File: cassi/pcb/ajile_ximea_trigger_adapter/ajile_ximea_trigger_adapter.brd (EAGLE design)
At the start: 27.9 x 57.6 mm, 10 parts, among them K1 694108105102

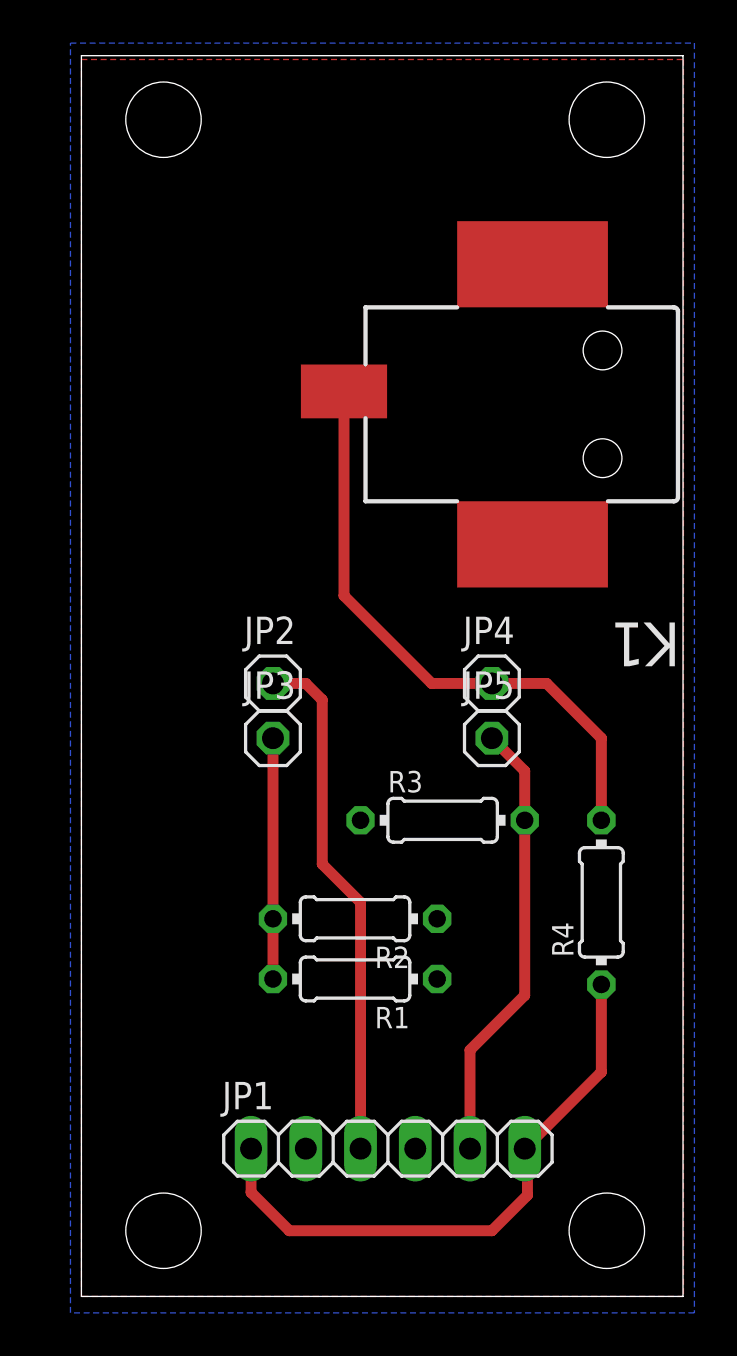
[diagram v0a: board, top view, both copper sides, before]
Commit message: put barrel jack on other side
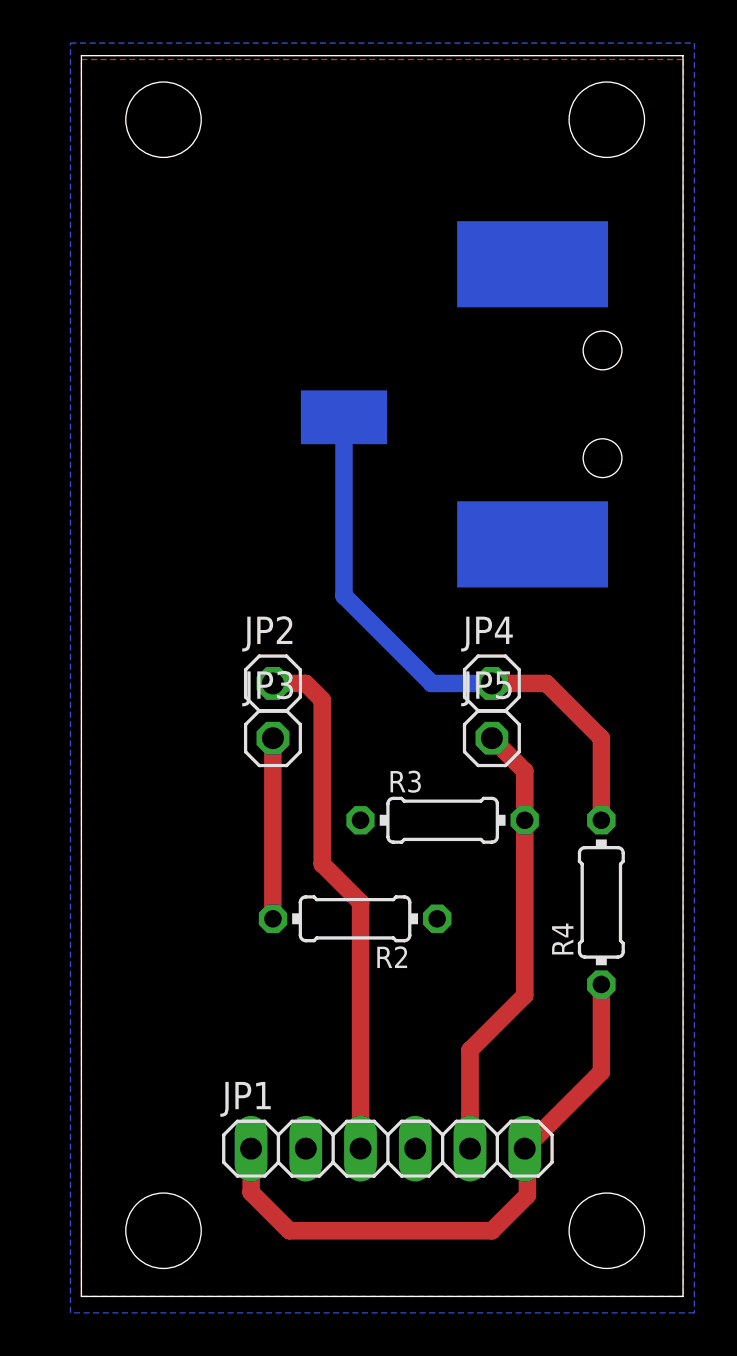
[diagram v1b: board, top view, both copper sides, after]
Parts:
- removed R1: 100, rcl:0204/7
- flipped K1 to the bottom, turned to 0 degrees
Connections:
- new net N$1: K1.2
- new net N$3: K1.3
- net GND: no longer K1.2, K1.3, R1.1
- net N$2: no longer R1.2
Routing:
- net N$2: track 11.2 -> 8.38 mm
- net 5V: track 28.0 -> 26.8 mm
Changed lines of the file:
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@@
 <elements>
 <element name="JP1" library="pinhead" library_urn="urn:adsk.eagle:library:325" package="1X06" package3d_urn="urn:adsk.eagle:package:22472/2" value="" x="14.224" y="6.858"/>
-<element name="K1" library="Wurth_Elektronik_Electromechanic_DC_Power_Jack_Connectors_rev15c" package="694108105102" value="694108105102" x="27.686" y="41.402" rot="R180"/>
+<element name="K1" library="Wurth_Elektronik_Electromechanic_DC_Power_Jack_Connectors_rev15c" package="694108105102" value="694108105102" x="27.686" y="41.402" rot="MR0"/>
 <element name="JP2" library="pinhead" library_urn="urn:adsk.eagle:library:325" package="1X01" package3d_urn="urn:adsk.eagle:package:22485/2" value="" x="8.89" y="28.448"/>
 <element name="JP3" library="pinhead" library_urn="urn:adsk.eagle:library:325" package="1X01" package3d_urn="urn:adsk.eagle:package:22485/2" value="" x="8.89" y="25.908"/>
 <element name="JP4" library="pinhead" library_urn="urn:adsk.eagle:library:325" package="1X01" package3d_urn="urn:adsk.eagle:package:22485/2" value="" x="19.05" y="28.448"/>
 <element name="JP5" library="pinhead" library_urn="urn:adsk.eagle:library:325" package="1X01" package3d_urn="urn:adsk.eagle:package:22485/2" value="" x="19.05" y="25.908"/>
-<element name="R1" library="rcl" library_urn="urn:adsk.eagle:library:334" package="0204/7" package3d_urn="urn:adsk.eagle:package:23498/1" value="100" x="12.7" y="14.732" rot="R180">
-<attribute name="SPICEPREFIX" value="R" x="12.7" y="14.732" size="1.778" layer="27" rot="R180" display="off"/>
-</element>
 <element name="R2" library="rcl" library_urn="urn:adsk.eagle:library:334" package="0204/7" package3d_urn="urn:adsk.eagle:package:23498/1" value="100" x="12.7" y="17.526" rot="R180">
 <attribute name="SPICEPREFIX" value="R" x="12.7" y="17.526" size="1.778" layer="27" rot="R180" display="off"/>
@@
 <contactref element="JP5" pad="1"/>
 <contactref element="R3" pad="2"/>
-<wire x1="20.574" y1="22.098" x2="20.574" y2="24.384" width="0.508" layer="1"/>
-<wire x1="20.574" y1="24.384" x2="19.05" y2="25.908" width="0.508" layer="1"/>
-<wire x1="20.574" y1="22.098" x2="20.574" y2="13.97" width="0.508" layer="1"/>
-<wire x1="20.574" y1="13.97" x2="18.034" y2="11.43" width="0.508" layer="1"/>
-<wire x1="18.034" y1="11.43" x2="18.034" y2="6.858" width="0.508" layer="1"/>
+<wire x1="20.574" y1="22.098" x2="20.574" y2="24.384" width="0.8128" layer="1"/>
+<wire x1="20.574" y1="24.384" x2="19.05" y2="25.908" width="0.8128" layer="1"/>
+<wire x1="20.574" y1="22.098" x2="20.574" y2="13.97" width="0.8128" layer="1"/>
+<wire x1="20.574" y1="13.97" x2="18.034" y2="11.43" width="0.8128" layer="1"/>
+<wire x1="18.034" y1="11.43" x2="18.034" y2="6.858" width="0.8128" layer="1"/>
 </signal>
 <signal name="AJILE_OUT">
 <contactref element="JP1" pad="3"/>
 <contactref element="JP2" pad="1"/>
-<wire x1="8.89" y1="28.448" x2="10.414" y2="28.448" width="0.508" layer="1"/>
-<wire x1="10.414" y1="28.448" x2="11.176" y2="27.686" width="0.508" layer="1"/>
-<wire x1="11.176" y1="27.686" x2="11.176" y2="20.066" width="0.508" layer="1"/>
-<wire x1="11.176" y1="20.066" x2="12.954" y2="18.288" width="0.508" layer="1"/>
-<wire x1="12.954" y1="18.288" x2="12.954" y2="6.858" width="0.508" layer="1"/>
+<wire x1="8.89" y1="28.448" x2="10.414" y2="28.448" width="0.8128" layer="1"/>
+<wire x1="10.414" y1="28.448" x2="11.176" y2="27.686" width="0.8128" layer="1"/>
+<wire x1="11.176" y1="27.686" x2="11.176" y2="20.066" width="0.8128" layer="1"/>
+<wire x1="11.176" y1="20.066" x2="12.954" y2="18.288" width="0.8128" layer="1"/>
+<wire x1="12.954" y1="18.288" x2="12.954" y2="6.858" width="0.8128" layer="1"/>
 </signal>
 <signal name="AJILE_IN">
@@
 <contactref element="JP1" pad="6"/>
 <contactref element="R4" pad="1"/>
-<wire x1="24.13" y1="14.478" x2="24.13" y2="10.414" width="0.508" layer="1"/>
-<wire x1="24.13" y1="10.414" x2="20.701" y2="6.985" width="0.508" layer="1"/>
+<wire x1="24.13" y1="14.478" x2="24.13" y2="10.414" width="0.8128" layer="1"/>
+<wire x1="24.13" y1="10.414" x2="20.701" y2="6.985" width="0.8128" layer="1"/>
 <wire x1="20.701" y1="6.985" x2="20.574" y2="6.858" width="0.508" layer="1"/>
-<wire x1="7.874" y1="6.858" x2="7.874" y2="4.826" width="0.508" layer="1"/>
-<wire x1="7.874" y1="4.826" x2="9.652" y2="3.048" width="0.508" layer="1"/>
-<wire x1="9.652" y1="3.048" x2="19.05" y2="3.048" width="0.508" layer="1"/>
-<wire x1="20.701" y1="4.699" x2="20.701" y2="6.985" width="0.508" layer="1"/>
-<wire x1="19.05" y1="3.048" x2="20.701" y2="4.699" width="0.508" layer="1"/>
+<wire x1="7.874" y1="6.858" x2="7.874" y2="4.826" width="0.8128" layer="1"/>
+<wire x1="7.874" y1="4.826" x2="9.652" y2="3.048" width="0.8128" layer="1"/>
+<wire x1="9.652" y1="3.048" x2="19.05" y2="3.048" width="0.8128" layer="1"/>
+<wire x1="20.701" y1="4.699" x2="20.701" y2="6.985" width="0.8128" layer="1"/>
+<wire x1="19.05" y1="3.048" x2="20.701" y2="4.699" width="0.8128" layer="1"/>
 </signal>
 <signal name="GND">
-<contactref element="K1" pad="2"/>
-<contactref element="K1" pad="3"/>
 <contactref element="JP1" pad="4"/>
 <contactref element="JP1" pad="2"/>
-<contactref element="R1" pad="1"/>
 <contactref element="R2" pad="1"/>
 <contactref element="R3" pad="1"/>
@@
 <contactref element="JP4" pad="1"/>
 <contactref element="R4" pad="2"/>
-<wire x1="12.186" y1="42.002" x2="12.186" y2="32.518" width="0.508" layer="1"/>
-<wire x1="12.186" y1="32.518" x2="16.256" y2="28.448" width="0.508" layer="1"/>
-<wire x1="16.256" y1="28.448" x2="19.05" y2="28.448" width="0.508" layer="1"/>
-<wire x1="19.05" y1="28.448" x2="21.59" y2="28.448" width="0.508" layer="1"/>
-<wire x1="21.59" y1="28.448" x2="24.13" y2="25.908" width="0.508" layer="1"/>
-<wire x1="24.13" y1="25.908" x2="24.13" y2="22.098" width="0.508" layer="1"/>
+<wire x1="12.186" y1="40.802" x2="12.186" y2="32.518" width="0.8128" layer="16"/>
+<wire x1="19.05" y1="28.448" x2="21.59" y2="28.448" width="0.8128" layer="1"/>
+<wire x1="21.59" y1="28.448" x2="24.13" y2="25.908" width="0.8128" layer="1"/>
+<wire x1="24.13" y1="25.908" x2="24.13" y2="22.098" width="0.8128" layer="1"/>
+<wire x1="12.186" y1="32.518" x2="16.256" y2="28.448" width="0.8128" layer="16"/>
+<wire x1="16.256" y1="28.448" x2="19.05" y2="28.448" width="0.8128" layer="16"/>
 </signal>
 <signal name="N$2">
-<contactref element="R1" pad="2"/>
 <contactref element="R2" pad="2"/>
 <contactref element="JP3" pad="1"/>
-<wire x1="8.89" y1="25.908" x2="8.89" y2="17.526" width="0.508" layer="1"/>
-<wire x1="8.89" y1="17.526" x2="8.89" y2="14.732" width="0.508" layer="1"/>
+<wire x1="8.89" y1="25.908" x2="8.89" y2="17.526" width="0.8128" layer="1"/>
+</signal>
+<signal name="N$1">
+<contactref element="K1" pad="2"/>
+</signal>
+<signal name="N$3">
+<contactref element="K1" pad="3"/>
 </signal>
 </signals>

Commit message: finished new ajile adapter pcb and added libraries used
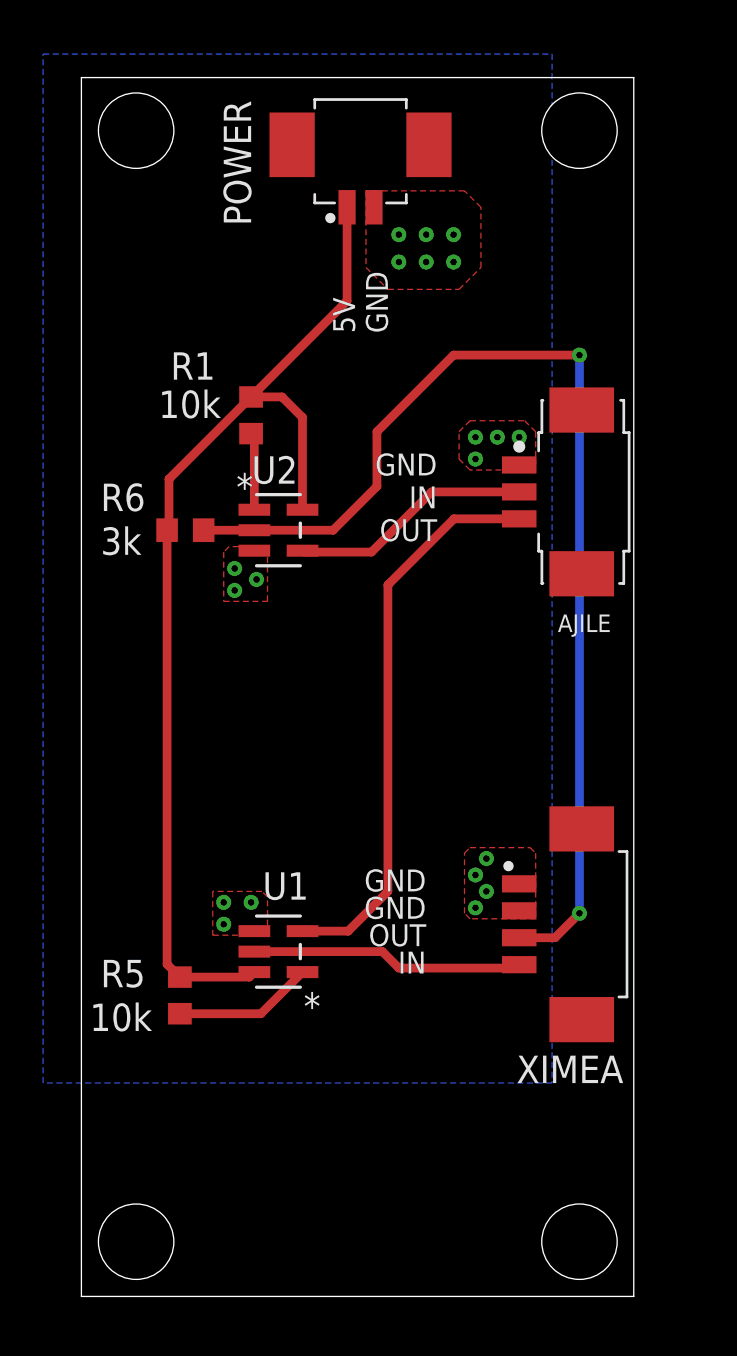
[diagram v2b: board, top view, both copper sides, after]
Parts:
- removed JP1: (no value), pinhead:1X06
- removed JP2, JP3, JP4, JP5: (no value), pinhead:1X01
- removed K1: 694108105102, Wurth_Elektronik_Electromechanic_DC_Power_Jack_Connectors_rev15c:694108105102
- removed R2: 100, rcl:0204/7
- removed R3: 2.2k, rcl:0204/7
- removed R4: 1k, rcl:0204/7
- added AJILE: 0532610371, 0532610371:MOLEX_0532610371
- added POWER: 0532610271, 0532610271:MOLEX_0532610271
- added R1, R5: 10k, resistor:R0603
- added R6: 3k, resistor:R0603
- added U1: SN74AHCT1G08DBVR, sn74ahct:DBV5
- added U2: SN74AHCT1G00DBVR, sn74ahct1g00:DBV5
- added XIMEA: 0532610471, 0532610471:MOLEX_0532610471
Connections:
- removed net 5V: JP4.1, K1.1, R4.2
- removed net N$1: K1.2
- removed net N$2: JP3.1, R2.2
- removed net N$3: K1.3
- new net 5VIN: POWER.1, R1.1, R5.1, R6.1, U1.5, U2.5
- new net N$4: R1.2, U2.1
- new net N$6: R5.2, U1.1
- new net XIMEA_OUT: R6.2, U2.2, XIMEA.3
- net AJILE_IN: now also AJILE.2, U2.4; no longer JP1.1, JP1.6, R4.1
- net AJILE_OUT: now also AJILE.3, U1.2; no longer JP1.3, JP2.1
- net GND: now also AJILE.1, POWER.2, U1.3, U2.3, XIMEA.1, XIMEA.2; no longer JP1.2, JP1.4, R2.1, R3.1
- net XIMEA_IN: now also U1.4, XIMEA.4; no longer JP1.5, JP5.1, R3.2
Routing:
- net XIMEA_OUT: track 0.00 -> 51.5 mm, vias 0 -> 2
- net 5VIN: track 0.00 -> 50.0 mm
- net 5V: track 26.8 -> 0.00 mm
- net AJILE_IN: track 27.7 -> 11.2 mm
- net N$2: track 8.38 -> 0.00 mm
- net XIMEA_IN: track 20.7 -> 12.7 mm
- net N$6: track 0.00 -> 6.49 mm
- net N$4: track 0.00 -> 3.60 mm
- net AJILE_OUT: track 24.2 -> 26.3 mm
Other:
- board size 27.9 x 57.6 mm -> 25.6 x 56.6 mm
- board text added: "5V"
- board text added: "Ajile <-> XIMEA Trigger Interface Matt Ruffner University of Kentucky 2018"
- board text added: "GND"
- board text added: "IN"
- board text added: "OUT"

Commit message: added final revisions to ximea trigger board
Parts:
- removed U1: SN74AHCT1G08DBVR, sn74ahct:DBV5
- added C1: 1uF, rcl:C0603
- added SN7408: SN74AHCT1G00DBVR, sn74ahct1g00:DBV5
- moved R5 7.68 mm to (8.89, 20.3), turned to 180 degrees
- moved POWER 0.51 mm to (13.0, 51.1)
- renumbered U2 to SN7400
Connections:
- removed net N$6: R5.2, U1.1
- new net N$1: R5.2, SN7408.1
- net 5VIN: now also C1.2, SN7408.5; no longer U1.5
- net AJILE_OUT: now also SN7408.2; no longer U1.2
- net GND: now also C1.1, SN7408.3; no longer U1.3
- net XIMEA_IN: now also SN7408.4; no longer U1.4
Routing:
- net N$6: track 6.49 -> 0.00 mm
- net N$1: track 0.00 -> 3.12 mm
- net XIMEA_IN: track 12.7 -> 10.2 mm
- net AJILE_OUT: track 26.3 -> 28.8 mm
- net XIMEA_OUT: track 51.5 -> 53.8 mm
- net 5VIN: track 50.0 -> 48.4 mm
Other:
- outline, holes or cut-outs redrawn
- board text added: "G"
- board text added: "XIMEA Trigger Interface v1.3 Matt Ruffner December 2018 University of Kentucky"
- board text removed: "Ajile <-> XIMEA Trigger Interface Matt Ruffner University of Kentucky 2018"
